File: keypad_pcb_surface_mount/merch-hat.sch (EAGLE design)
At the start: 15 parts

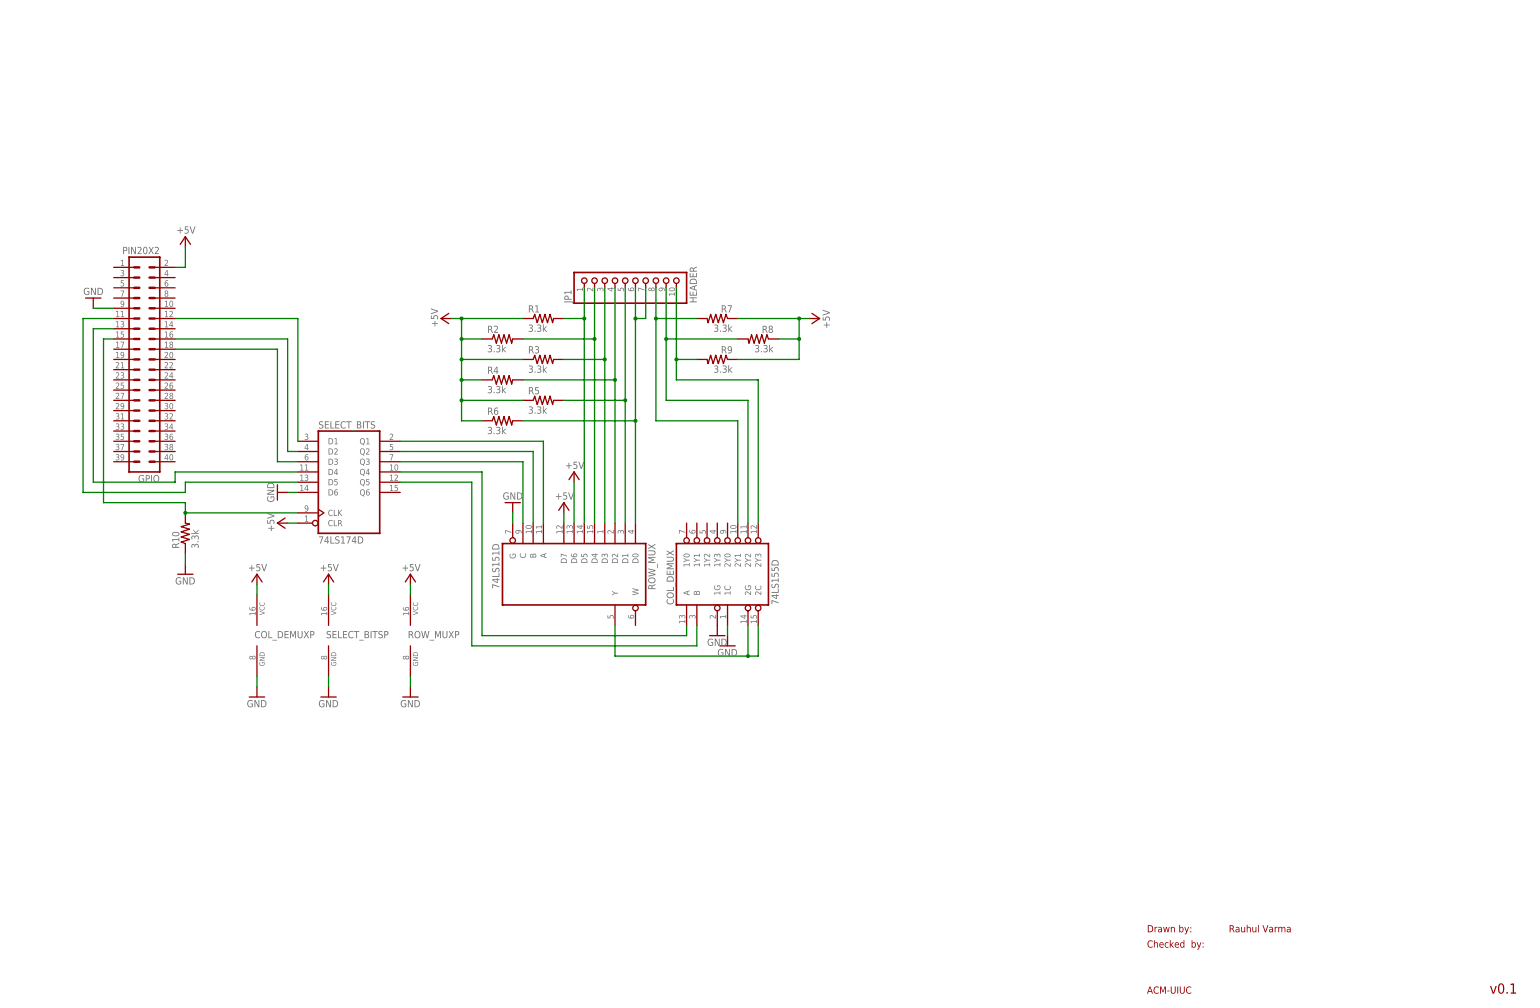
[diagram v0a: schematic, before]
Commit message: Move Keypad, Add Port Sensor
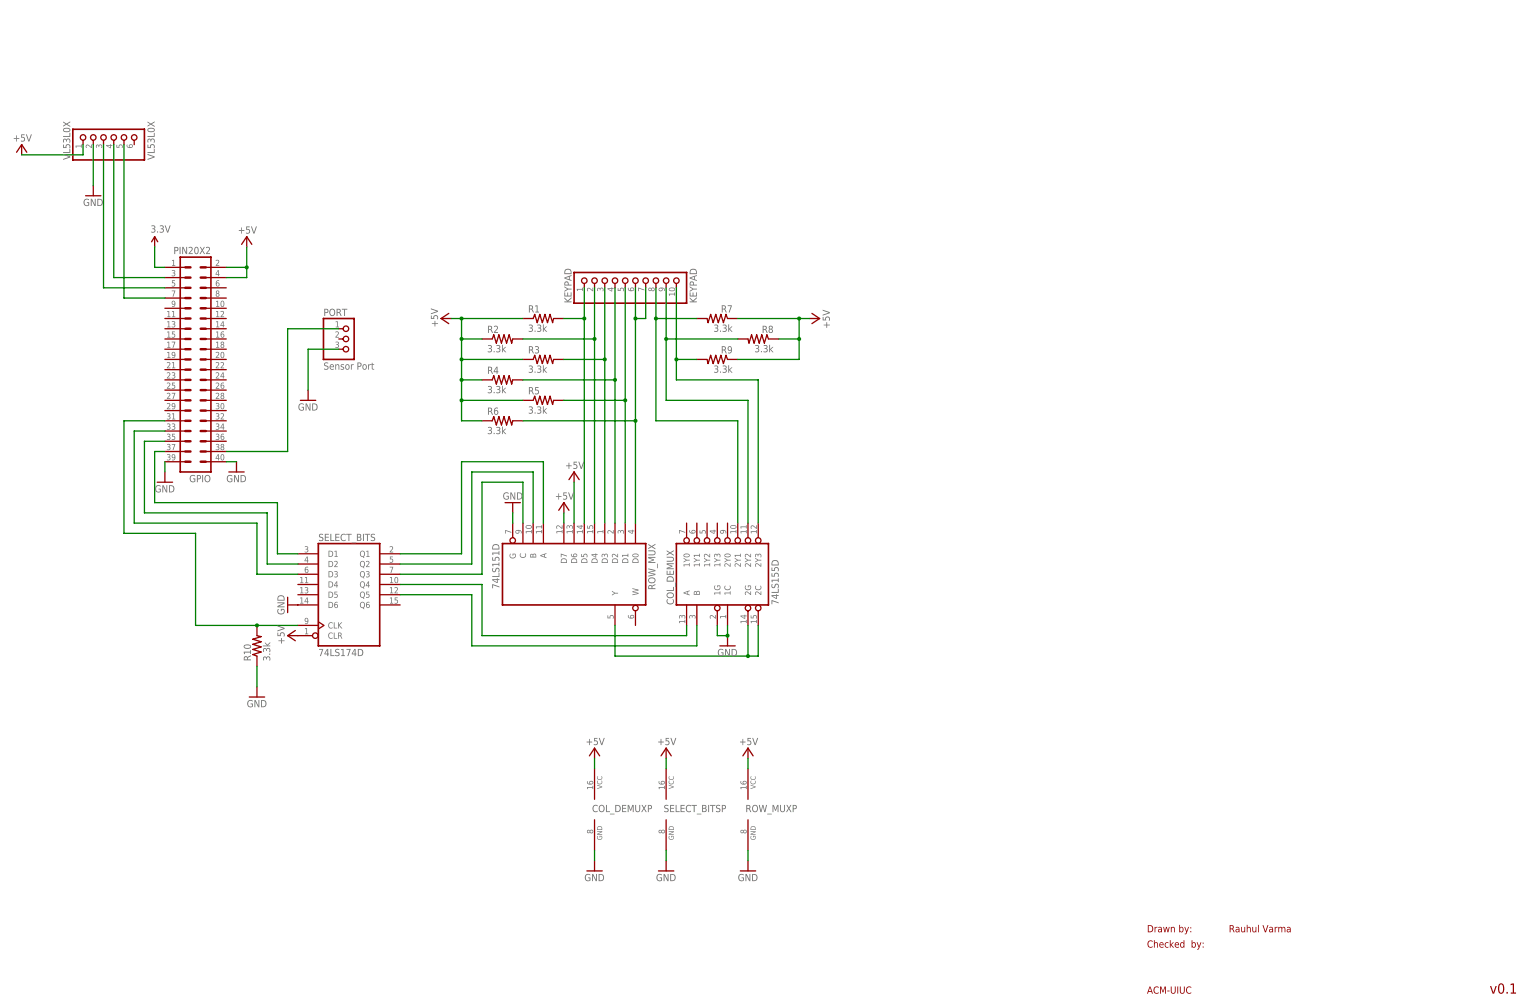
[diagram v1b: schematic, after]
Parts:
- added PORT: Sensor Port, pinhead:PINHD-1X3
- added VL53L0X: VL53L0X, pinhead:PINHD-1X6
- KEYPAD: value HEADER -> KEYPAD
- renumbered JP1 to KEYPAD
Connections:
- removed net N$7: GPIO.11, SELECT_BITSA.D5
- removed net N$8: GPIO.15, R10.2, SELECT_BITSA.CLK
- new net 3.3V: GPIO.1
- new net 5V: COL_DEMUXP.GND, ROW_MUXP.GND, SELECT_BITSA.D6, SELECT_BITSP.GND
- new net CLK: GPIO.31, R10.2, SELECT_BITSA.CLK
- new net N$19: GPIO.5, VL53L0X.3
- new net N$23: GPIO.3, VL53L0X.4
- new net N$24: GPIO.7, VL53L0X.5
- net +5V: now also GPIO.4, VL53L0X.1
- net GND: now also GPIO.39, GPIO.40, PORT.3, VL53L0X.2; no longer COL_DEMUXP.GND, GPIO.9, ROW_MUXP.GND, SELECT_BITSA.D6, SELECT_BITSP.GND
- net N$2: now also GPIO.33, SELECT_BITSA.D3; no longer GPIO.16, SELECT_BITSA.D2
- net N$3: now also GPIO.35, SELECT_BITSA.D2; no longer GPIO.18, SELECT_BITSA.D3
- net N$5: now also GPIO.37, SELECT_BITSA.D1; no longer GPIO.13, SELECT_BITSA.D4
- net N$6: now also GPIO.38, PORT.1; no longer GPIO.12, SELECT_BITSA.D1
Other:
- moved on the sheet: COL_DEMUXP, GPIO, R10, ROW_MUXP, SELECT_BITS, SELECT_BITSP

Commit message: Finish Up Surface Mount Version
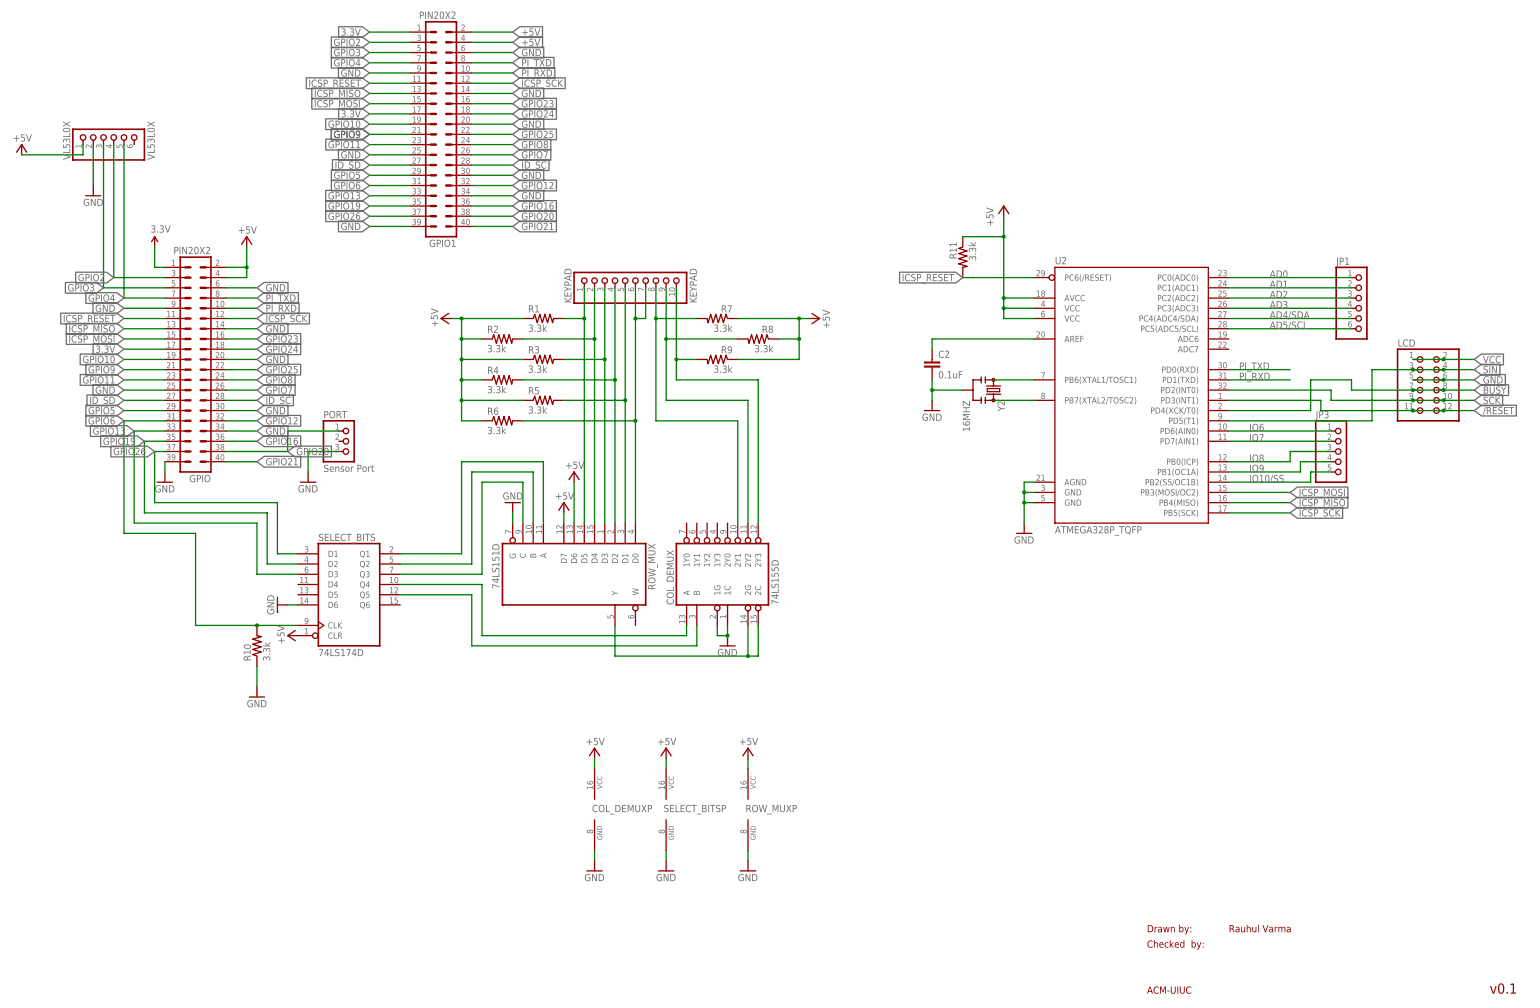
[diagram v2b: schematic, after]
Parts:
- added C2: 0.1uF, SparkFun-Capacitors:CAP0603-CAP
- added GPIO1: PIN20X2, FLYFISH:PIN20X2
- added JP1: (no value), pinhead:PINHD-1X6
- added JP3: (no value), pinhead:PINHD-1X5
- added LCD: (no value), pinhead:PINHD-2X6
- added R11: 3.3k, resistor:R-US_R0805
- added U2: ATMEGA328P_TQFP, SparkFun-DigitalIC:ATMEGA328P_TQFP
- added Y2: 16MHZ, SparkFun-FreqCtrl:RESONATOR16MHZ
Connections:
- removed net 5V: COL_DEMUXP.GND, ROW_MUXP.GND, SELECT_BITSA.D6, SELECT_BITSP.GND
- removed net CLK: GPIO.31, R10.2, SELECT_BITSA.CLK
- removed net N$19: GPIO.5, VL53L0X.3
- removed net N$2: GPIO.33, SELECT_BITSA.D3
- removed net N$23: GPIO.3, VL53L0X.4
- removed net N$24: GPIO.7, VL53L0X.5
- removed net N$3: GPIO.35, SELECT_BITSA.D2
- removed net N$5: GPIO.37, SELECT_BITSA.D1
- removed net N$6: GPIO.38, PORT.1
- new net /RESET: LCD.11, LCD.12, U2.PD3(INT1)
- new net AD0: JP1.1, U2.PC0(ADC0)
- new net AD1: JP1.2, U2.PC1(ADC1)
- new net AD2: JP1.3, U2.PC2(ADC2)
- new net AD3: JP1.4, U2.PC3(ADC3)
- new net AD4/SDA: JP1.5, U2.PC4(ADC4/SDA)
- new net AD5/SCL: JP1.6, U2.PC5(ADC5/SCL)
- new net BUSY: LCD.7, LCD.8, U2.PD4(XCK/T0)
- new net GPIO10: GPIO.19, GPIO1.19
- new net GPIO11: GPIO.23, GPIO1.23
- new net GPIO12: GPIO.32, GPIO1.32
- new net GPIO13: GPIO.33, GPIO1.33, SELECT_BITSA.D3
- new net GPIO16: GPIO.36, GPIO1.36
- new net GPIO19: GPIO.35, GPIO1.35, SELECT_BITSA.D2
- new net GPIO2: GPIO.3, GPIO1.3, VL53L0X.4
- new net GPIO20: GPIO.38, GPIO1.38, PORT.1
- new net GPIO21: GPIO.40, GPIO1.40
- new net GPIO23: GPIO.16, GPIO1.16
- new net GPIO24: GPIO.18, GPIO1.18
- new net GPIO25: GPIO.22, GPIO1.22
- new net GPIO26: GPIO.37, GPIO1.37, SELECT_BITSA.D1
- new net GPIO3: GPIO.5, GPIO1.5, VL53L0X.3
- new net GPIO4: GPIO.7, GPIO1.7, VL53L0X.5
- new net GPIO5: GPIO.29, GPIO1.29
- new net GPIO6: GPIO.31, GPIO1.31, R10.2, SELECT_BITSA.CLK
- new net GPIO7: GPIO.26, GPIO1.26
- new net GPIO8: GPIO.24, GPIO1.24
- new net GPIO9: GPIO.21, GPIO1.21
- new net ICSP_MISO: GPIO.13, GPIO1.13, U2.PB4(MISO)
- new net ICSP_MOSI: GPIO.15, GPIO1.15, U2.PB3(MOSI/OC2)
- new net ICSP_RESET: GPIO.11, GPIO1.11, R11.2, U2.PC6(/RESET)
- new net ICSP_SCK: GPIO.12, GPIO1.12, U2.PB5(SCK)
- new net ID_SC: GPIO.28, GPIO1.28
- new net ID_SD: GPIO.27, GPIO1.27
- new net IO10/SS: JP3.5, U2.PB2(SS/OC1B)
- new net IO6: JP3.1, U2.PD6(AIN0)
- new net IO7: JP3.2, U2.PD7(AIN1)
- new net IO8: JP3.3, U2.PB0(ICP)
- new net IO9: JP3.4, U2.PB1(OC1A)
- new net N$29: U2.PB6(XTAL1/TOSC1), Y2.1
- new net N$30: U2.PB7(XTAL2/TOSC2), Y2.3
- new net N$32: C2.1, U2.AREF
- new net PI_RXD: GPIO.10, GPIO1.10, U2.PD1(TXD)
- new net PI_TXD: GPIO.8, GPIO1.8, U2.PD0(RXD)
- new net SCK: LCD.10, LCD.9, U2.PD2(INT0)
- new net SIN: LCD.3, LCD.4, U2.PD5(T1)
- new net VCC: LCD.1, LCD.2
- net +5V: now also GPIO1.2, GPIO1.4, R11.1, U2.AVCC, U2.VCC@4, U2.VCC@6
- net 3.3V: now also GPIO.17, GPIO1.1, GPIO1.17
- net GND: now also C2.2, COL_DEMUXP.GND, GPIO.14, GPIO.20, GPIO.25, GPIO.30, GPIO.34, GPIO.6, GPIO.9, GPIO1.14, GPIO1.20, GPIO1.25, GPIO1.30, GPIO1.34, GPIO1.39, GPIO1.6, GPIO1.9, LCD.5, LCD.6, ROW_MUXP.GND, SELECT_BITSA.D6, SELECT_BITSP.GND, U2.AGND, U2.GND@3, U2.GND@5, Y2.2; no longer GPIO.40
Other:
- moved on the sheet: PORT

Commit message: add decoupling cap
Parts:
- added C1: 0.1uF, SparkFun-Capacitors:CAP0603-CAP
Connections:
- net +5V: now also C1.1
- net GND: now also C1.2
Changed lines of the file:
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@@
 <?xml version="1.0" encoding="utf-8"?>
 <!DOCTYPE eagle SYSTEM "eagle.dtd">
-<eagle version="8.1.0">
+<eagle version="8.0.1">
 <drawing>
 <settings>
@@
 <part name="JP3" library="pinhead" deviceset="PINHD-1X5" device=""/>
 <part name="R11" library="resistor" deviceset="R-US_" device="R0805" value="3.3k"/>
+<part name="C1" library="SparkFun-Capacitors" deviceset="CAP" device="0603-CAP" value="0.1uF"/>
+<part name="GND4" library="supply1" deviceset="GND" device=""/>
+<part name="P+11" library="supply1" deviceset="+5V" device=""/>
 </parts>
 <sheets>
@@
 <instance part="JP3" gate="A" x="337.82" y="139.7"/>
 <instance part="R11" gate="G$1" x="243.84" y="187.96" rot="MR270"/>
+<instance part="C1" gate="G$1" x="213.36" y="43.18"/>
+<instance part="GND4" gate="1" x="213.36" y="35.56"/>
+<instance part="P+11" gate="1" x="213.36" y="53.34" smashed="yes">
+<attribute name="VALUE" x="215.9" y="55.88" size="1.778" layer="96" rot="R180"/>
+</instance>
 </instances>
 <busses>
@@
 <junction x="66.04" y="185.42"/>
 </segment>
+<segment>
+<pinref part="C1" gate="G$1" pin="1"/>
+<pinref part="P+11" gate="1" pin="+5V"/>
+<wire x1="213.36" y1="50.8" x2="213.36" y2="48.26" width="0.1524" layer="91"/>
+</segment>
 </net>
 <net name="GPIO6" class="0">
@@
 <label x="132.08" y="203.2" size="1.778" layer="95" xref="yes"/>
 </segment>
-</net>
+<segment>
+<pinref part="C1" gate="G$1" pin="2"/>
+<pinref part="GND4" gate="1" pin="GND"/>
+<wire x1="213.36" y1="38.1" x2="213.36" y2="40.64" width="0.1524" layer="91"/>
+</segment>
+</net>

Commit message: Add Limit Switch Interface
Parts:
- added LIMITSWITCH: (no value), pinhead:PINHD-1X2
- added R12, R13: 3.3k, resistor:R-US_R0805
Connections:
- net +5V: now also R12.1, R13.1
- net GPIO23: now also LIMITSWITCH.2, R12.2
- net GPIO24: now also LIMITSWITCH.1, R13.2
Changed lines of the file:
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@@
 <?xml version="1.0" encoding="utf-8"?>
 <!DOCTYPE eagle SYSTEM "eagle.dtd">
-<eagle version="8.0.1">
+<eagle version="8.1.0">
 <drawing>
 <settings>
@@
 <part name="GND4" library="supply1" deviceset="GND" device=""/>
 <part name="P+11" library="supply1" deviceset="+5V" device=""/>
+<part name="R12" library="resistor" deviceset="R-US_" device="R0805" value="3.3k"/>
+<part name="P+13" library="supply1" deviceset="+5V" device=""/>
+<part name="R13" library="resistor" deviceset="R-US_" device="R0805" value="3.3k"/>
+<part name="P+14" library="supply1" deviceset="+5V" device=""/>
+<part name="LIMITSWITCH" library="pinhead" deviceset="PINHD-1X2" device=""/>
 </parts>
 <sheets>
@@
 <attribute name="VALUE" x="215.9" y="55.88" size="1.778" layer="96" rot="R180"/>
 </instance>
+<instance part="R12" gate="G$1" x="172.72" y="231.14" rot="MR270"/>
+<instance part="P+13" gate="1" x="172.72" y="238.76" smashed="yes">
+<attribute name="VALUE" x="175.26" y="241.3" size="1.778" layer="96" rot="R180"/>
+</instance>
+<instance part="R13" gate="G$1" x="190.5" y="228.6" rot="MR270"/>
+<instance part="P+14" gate="1" x="190.5" y="236.22" smashed="yes">
+<attribute name="VALUE" x="193.04" y="238.76" size="1.778" layer="96" rot="R180"/>
+</instance>
+<instance part="LIMITSWITCH" gate="G$1" x="165.1" y="210.82" rot="R270"/>
 </instances>
 <busses>
@@
 <wire x1="213.36" y1="50.8" x2="213.36" y2="48.26" width="0.1524" layer="91"/>
 </segment>
+<segment>
+<pinref part="R12" gate="G$1" pin="1"/>
+<pinref part="P+13" gate="1" pin="+5V"/>
+</segment>
+<segment>
+<pinref part="R13" gate="G$1" pin="1"/>
+<pinref part="P+14" gate="1" pin="+5V"/>
+</segment>
 </net>
 <net name="GPIO6" class="0">
@@
 <segment>
 <pinref part="GPIO1" gate="G$1" pin="18"/>
-<wire x1="121.92" y1="223.52" x2="132.08" y2="223.52" width="0.1524" layer="91"/>
 <label x="132.08" y="223.52" size="1.778" layer="95" xref="yes"/>
+<pinref part="R13" gate="G$1" pin="2"/>
+<wire x1="190.5" y1="226.06" x2="190.5" y2="223.52" width="0.1524" layer="91"/>
+<wire x1="190.5" y1="223.52" x2="167.64" y2="223.52" width="0.1524" layer="91"/>
+<junction x="190.5" y="223.52"/>
+<pinref part="LIMITSWITCH" gate="G$1" pin="1"/>
+<wire x1="167.64" y1="223.52" x2="121.92" y2="223.52" width="0.1524" layer="91"/>
+<wire x1="167.64" y1="213.36" x2="167.64" y2="223.52" width="0.1524" layer="91"/>
+<junction x="167.64" y="223.52"/>
 </segment>
 </net>
@@
 <segment>
 <pinref part="GPIO1" gate="G$1" pin="16"/>
-<wire x1="121.92" y1="226.06" x2="132.08" y2="226.06" width="0.1524" layer="91"/>
 <label x="132.08" y="226.06" size="1.778" layer="95" xref="yes"/>
-</segment>
-</net>
+<pinref part="R12" gate="G$1" pin="2"/>
+<wire x1="172.72" y1="226.06" x2="165.1" y2="226.06" width="0.1524" layer="91"/>
+<pinref part="LIMITSWITCH" gate="G$1" pin="2"/>
+<wire x1="165.1" y1="226.06" x2="121.92" y2="226.06" width="0.1524" layer="91"/>
+<wire x1="165.1" y1="213.36" x2="165.1" y2="226.06" width="0.1524" layer="91"/>
+<junction x="165.1" y="226.06"/>
+</segment>
+</net>

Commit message: Fixes and updates
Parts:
- removed COL_DEMUX: 74LS155D, 74xx-us:74LS155D
- removed GPIO1: PIN20X2, FLYFISH:PIN20X2
- added C3: 0.1uF, merch-hardware:CAP0603-CAP
- added D2: 74LS156D, 74xx-us:74LS156D
- added R14: 1k, merch-hardware:RESISTOR0603-RES
- added R15, R16: 3.9k, merch-hardware:RESISTOR0603-RES
- added U1: CAT24C32, merch-hardware:CAT24C32
- added WP: (no value), pinhead:PINHD-1X2
- R1, R10, R11, R12, R13, R2, R3, R4, R5, R6, R7, R8, R9: device resistor:R-US_R0805 -> merch-hardware:RESISTOR0603
- renumbered PORT to PORT_OUT, ROW_MUX to D1, SELECT_BITS to D3
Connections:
- new net N$2: R14.1, U1.WP, WP.1
- net +5V: now also D2P.VCC; no longer COL_DEMUXP.VCC, GPIO1.2, GPIO1.4
- net 3.3V: now also C3.2, R14.2, R15.2, R16.2, U1.VCC; no longer GPIO1.1, GPIO1.17
- net GND: now also C3.1, D2A.1C, D2A.1G, D2A.2G, D2P.GND, U1.A0, U1.A1, U1.A2, U1.VSS, WP.2; no longer COL_DEMUXA.1C, COL_DEMUXA.1G, COL_DEMUXP.GND, GPIO1.14, GPIO1.20, GPIO1.25, GPIO1.30, GPIO1.34, GPIO1.39, GPIO1.6, GPIO1.9
- net GPIO10: no longer GPIO1.19
- net GPIO11: no longer GPIO1.23
- net GPIO12: no longer GPIO1.32
- net GPIO13: no longer GPIO1.33
- net GPIO16: now also D3A.D4; no longer GPIO1.36
- net GPIO19: no longer GPIO1.35
- net GPIO2: no longer GPIO1.3
- net GPIO20: no longer GPIO1.38
- net GPIO21: no longer GPIO1.40
- net GPIO23: now also LIMITSWITCH.1; no longer GPIO1.16, LIMITSWITCH.2
- net GPIO24: now also LIMITSWITCH.2; no longer GPIO1.18, LIMITSWITCH.1
- net GPIO25: no longer GPIO1.22
- net GPIO26: no longer GPIO1.37
- net GPIO3: no longer GPIO1.5
- net GPIO4: no longer GPIO1.7
- net GPIO5: now also D3A.D5; no longer GPIO1.29
- net GPIO6: no longer GPIO1.31
- net GPIO7: no longer GPIO1.26
- net GPIO8: no longer GPIO1.24
- net GPIO9: no longer GPIO1.21
- net ICSP_MISO: no longer GPIO1.13
- net ICSP_MOSI: no longer GPIO1.15
- net ICSP_RESET: no longer GPIO1.11
- net ICSP_SCK: no longer GPIO1.12
- net ID_SC: now also R15.1, U1.SCL; no longer GPIO1.28
- net ID_SD: now also R16.1, U1.SDA; no longer GPIO1.27
- net N$14: now also D2A.2Y1; no longer COL_DEMUXA.2Y1
- net N$15: now also D2A.2Y2; no longer COL_DEMUXA.2Y2
- net N$16: now also D2A.2Y3; no longer COL_DEMUXA.2Y3
- net N$20: now also D2A.A; no longer COL_DEMUXA.A
- net N$21: now also D2A.B; no longer COL_DEMUXA.B
- net N$22: now also D2A.2C; no longer COL_DEMUXA.2C, COL_DEMUXA.2G
- net PI_RXD: no longer GPIO1.10
- net PI_TXD: no longer GPIO1.8
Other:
- moved on the sheet: LIMITSWITCH, R12, R13

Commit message: add power connctor, new range sensor pinout, pullup
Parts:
- removed VL53L0X: VL53L0X, pinhead:PINHD-1X6
- added +5V: (no value), con-jack:JACK-PLUG1
- added CUP: (no value), pinhead:PINHD-1X7
- added R17: 1.5K, rcl:R-US_R0603
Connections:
- new net N$3: PORT_OUT.2, R17.1
- net +5V: now also +5V.3, CUP.1; no longer VL53L0X.1
- net GND: now also +5V.1, CUP.3; no longer VL53L0X.2
- net GPIO2: now also CUP.7; no longer VL53L0X.4
- net GPIO20: now also R17.2
- net GPIO3: now also CUP.6; no longer VL53L0X.3
- net GPIO4: now also CUP.4; no longer VL53L0X.5
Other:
- note added: "POWER IN"
- moved on the sheet: PORT_OUT
